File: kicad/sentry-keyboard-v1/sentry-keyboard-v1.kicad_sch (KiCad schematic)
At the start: 273 parts, among them J1 USB_C_Receptacle_USB2.0, J4 AVR-ISP-6, SW1 Reset, SW2 RotaryEncoder_Switch, U1 ATmega32U4-AU, U3 PRTR5V0U2X, Y1 16Mhz

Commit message: Move kicad library
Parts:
- D100, D101, D102, D103, D104, D105, D106, D107, D108, D109, D110, D111, D112, D113, D114, D115, D116, D117, D118, D119, D120, D121, D122, D123, D124, D125, D126, D127, D128, D129, D130, D131, D132, D133, D134, D135, D136, D137, D138, D139, D140, D141, D142, D143, D144, D145, D146, D147, D148, D149, D150, D151, D152, D153, D154, D155, D156, D157, D158, D159, D160, D161, D162, D163, D164, D83, D84, D85, D86, D87, D88, D89, D90, D91, D92, D93, D94, D95, D96, D97, D98, D99: footprint LED_SMD:LED_SK6812_PLCC4_5.0x5.0mm_P3.2mm -> Keebio:SK6812-MINI-E
- MXlshift1: footprint Keebio-Parts:MX-Alps-Choc-1U-NoLED -> Button_Switch_Keyboard:SW_Cherry_MX_1.75u_PCB
- MXspace1: footprint Keebio-Parts:MX-Alps-Choc-1U-NoLED -> Button_Switch_Keyboard:SW_Cherry_MX_6.25u_PCB
- SW1: footprint Keebio-Parts:SW_SPST_TL3342 -> Keebio:SW_SPST_TL3342
- SW2: footprint Rotary_Encoder:RotaryEncoder_Alps_EC11E-Switch_Vertical_H20mm_MountingHoles -> Keebio:RotaryEncoder_EC11
- U3: footprint Keebio-Parts:SOT-143B -> Keebio:SOT-143B

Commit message: Update schematic
- fix avr isp pin out
- add footprints to switches and leds
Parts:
- ESC1, F10, F11, F12, F13, F2, F3, F4, F5, F6, F7, F8, F9, MX'1, MX+1, MX,1, MX-1, MX.1, MX/1, MX0, MX1, MX2, MX3, MX4, MX5, MX6, MX7, MX8, MX9, MX;1, MX[1, MX\1, MX]1, MXa1, MXb1, MXc1, MXd1, MXdown1, MXe1, MXend1, MXf2, MXfn1, MXg1, MXh1, MXhome1, MXi1, MXj1, MXk1, MXl1, MXleft1, MXm1, MXn1, MXo1, MXp1, MXpgdn1, MXpgup1, MXq1, MXr1, MXright1, MXs1, MXt1, MXtilde1, MXu1, MXup1, MXv1, MXw1, MXx1, MXy1, MXz1: footprint Keebio-Parts:MX-Alps-Choc-1U-NoLED -> Kaihl hotswap:MX-Hotswap-1U
- F1: renamed from F1-1; footprint Keebio-Parts:MX-Alps-Choc-1U-NoLED -> Fuse:Fuse_1206_3216Metric_Pad1.42x1.75mm_HandSolder
- MXalt1, MXctrl1, MXralt1, MXrctrl1, MXsuper1: footprint Keebio-Parts:MX-Alps-Choc-1U-NoLED -> Kaihl hotswap:MX-Hotswap-1.25U
- MXbksp1: footprint Keebio-Parts:MX-Alps-Choc-1U-NoLED -> Kaihl hotswap:MX-Hotswap-2U
- MXcaps1, MXrshift1: footprint Keebio-Parts:MX-Alps-Choc-1U-NoLED -> Kaihl hotswap:MX-Hotswap-1.75U
- MXenter1, MXtab1: footprint Keebio-Parts:MX-Alps-Choc-1U-NoLED -> Kaihl hotswap:MX-Hotswap-1.5U
- MXlshift1: footprint Button_Switch_Keyboard:SW_Cherry_MX_1.75u_PCB -> Kaihl hotswap:MX-Hotswap-2U
- MXspace1: footprint Button_Switch_Keyboard:SW_Cherry_MX_6.25u_PCB -> Kaihl hotswap:MX-Hotswap-6.25U
- renumbered F1 to FU1
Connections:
- net Row2-L is gone; now on net Row1: J4.3 (SCK)
- net Col0: no longer J4.1 (MISO)
- net Col1: no longer J4.4 (MOSI)
- net Row2: now also J4.4 (MOSI)
- net Row3: now also J4.1 (MISO)

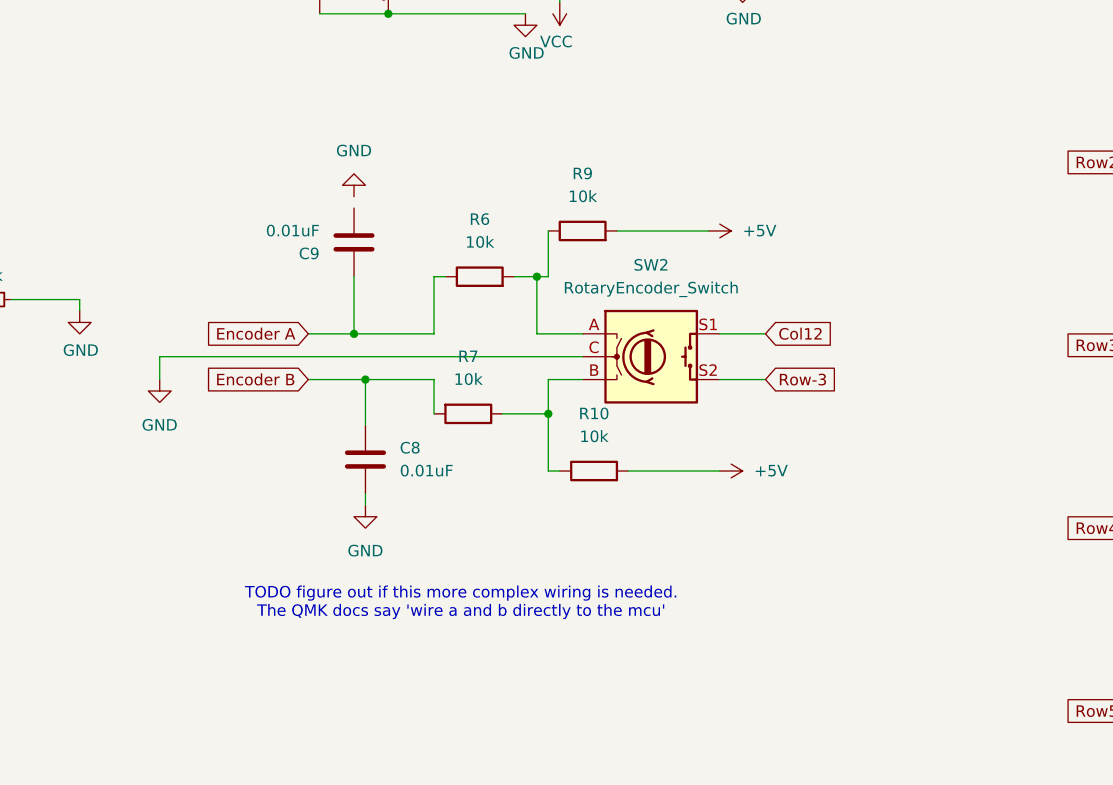
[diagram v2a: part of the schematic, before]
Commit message: Cleanup rotary encoder wiring
- forgot a diode
- don't need as many resistors. I looked at a couple other keyboards
  with rotary encoders and none of them had two sets of resistors.
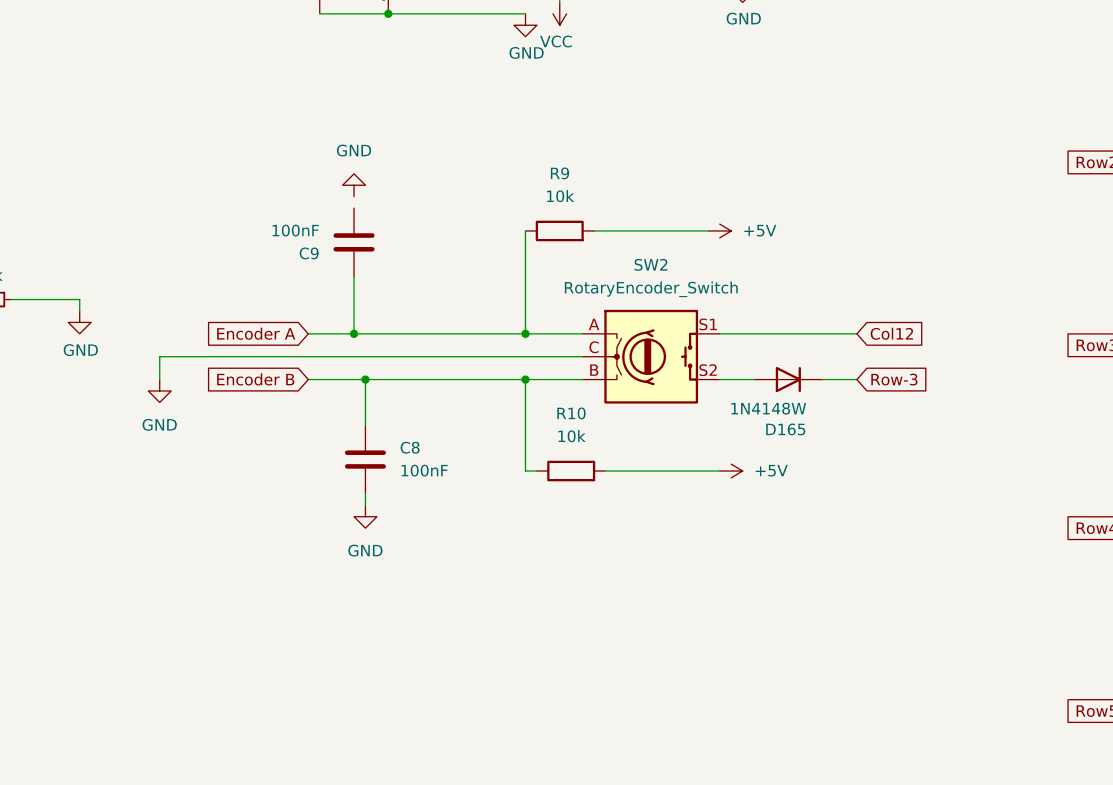
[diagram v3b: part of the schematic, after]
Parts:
- removed R6, R7: 10k, Resistor_SMD:R_0805_2012Metric, symbol Device:R
- added D165: 1N4148W, Diode_SMD:D_SOD-123, symbol Diode:1N4148W
- C8, C9: value 0.01uF -> 100nF
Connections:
- net Encoder A: now also R9.1, SW2.A
- net Encoder B: now also R10.1, SW2.B
- net Row-3: now also D165.1 (K); no longer SW2.S2
- new net: D165.2 (A), SW2.S2
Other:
- note removed: "TODO figure out if this more complex wiring is needed. The QMK docs say 'wire a and b directly to the mcu'"
- moved on the sheet: R10, R9

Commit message: Fix footprint
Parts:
- J4: footprint random-keyboard-parts:Reset_Pretty-Mask -> Keebio:Reset_Pretty-Mask
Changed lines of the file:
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@@
 			)
 		)
-		(property "Footprint" "random-keyboard-parts:Reset_Pretty-Mask"
+		(property "Footprint" "Keebio:Reset_Pretty-Mask"
 			(at 21.59 34.29 90)
 			(effects

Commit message: Add Mx_Alps_Hybrid library to get schematic symbols back
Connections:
- net Row-3 is gone; now on net Row3: D165.1 (K)
- net Col13: no longer names the net of U1.40 (PF1)
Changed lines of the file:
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@@
-		)
-	)
-	(global_label "Col13"
-		(shape input)
-		(at 96.52 113.03 0)
-		(fields_autoplaced yes)
-		(effects
-			(font
-				(size 1.27 1.27)
-			)
-			(justify left)
-		)
-		(property "Intersheetrefs" "${INTERSHEET_REFS}"
-			(at 105.0084 113.03 0)
-			(effects
-				(font
-					(size 1.27 1.27)
-				)
-				(justify left)
-				(hide yes)
-			)
 		)
 	)
@@
 		)
 	)
-	(global_label "Row-3"
+	(global_label "Row3"
 		(shape input)
 		(at 207.01 111.76 0)
@@
 		)
 		(property "Intersheetrefs" "${INTERSHEET_REFS}"
-			(at 216.5266 111.76 0)
+			(at 214.9542 111.76 0)
 			(effects
 				(font
